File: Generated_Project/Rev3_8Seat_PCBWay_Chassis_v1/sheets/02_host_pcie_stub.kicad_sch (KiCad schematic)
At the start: 0 parts

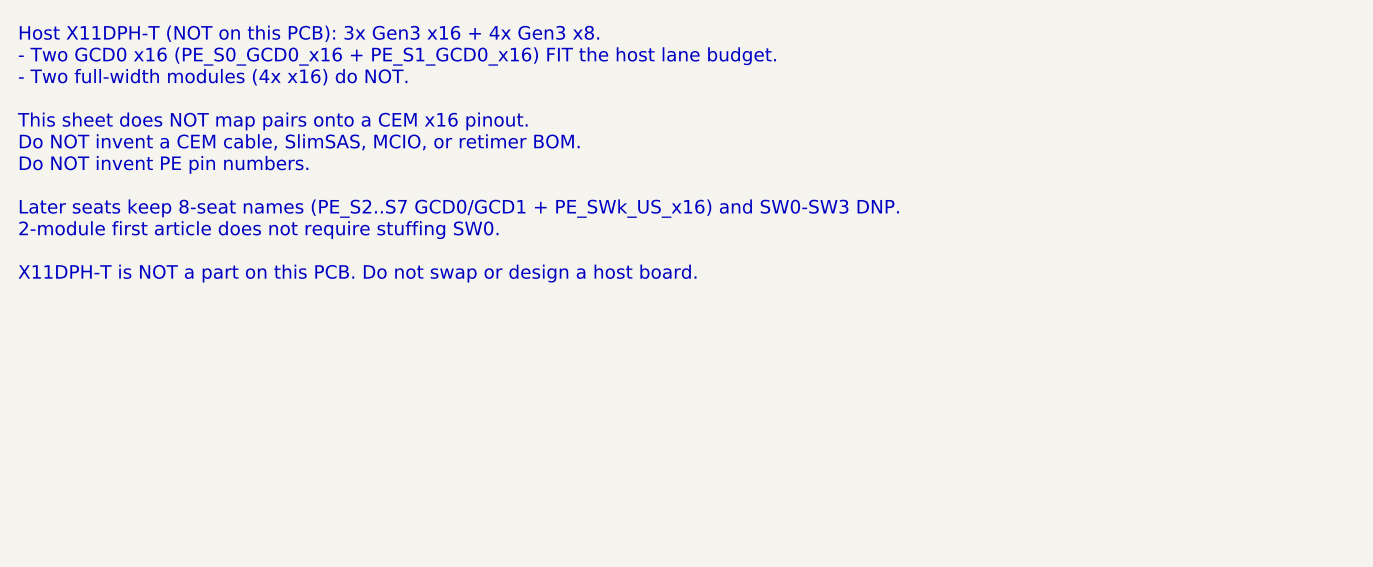
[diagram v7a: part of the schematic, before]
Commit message: Document an 8x full-width chassis CONCEPT (ideas only, not fab).
Sibling folder plus STATUS pointer. Comments-layer KiCad notes say
CONCEPT / DO NOT FABRICATE. No overlay, ball map, CEM/MCIO, r2.0, or
S1-S7 assignment. X11DPH-T cannot light 256 DS. Do not energize.
Do not upload to PCBWay.

Co-authored-by: zivzancoeli-commits <zivzancoeli-commits@users.noreply.github.com>
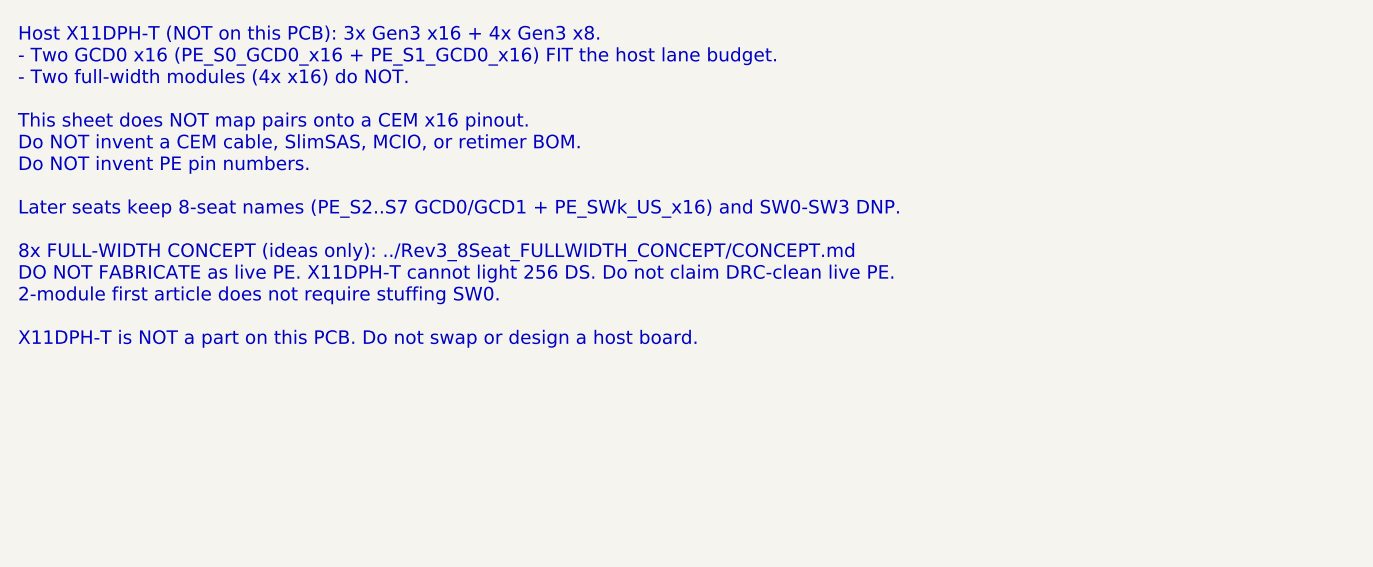
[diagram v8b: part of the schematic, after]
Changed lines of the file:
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@@
         (comment 4 "r2.0 UNUSABLE. P3V3=Conn0 C1/C2. 12L 2.0mm stuffed-switch TARGET. 4x PM8536 DNP. Star-fed P48V.")
 	)
-	(text "PURPOSE: Named v1.0 PCIE_TXnP/N and PCIE_RXnP/N (n=0..15) on ALL 8 seats.\n\nFIRST ARTICLE TARGET: seats 0 and 1. Same 8-seat PCB; 2→4→8 later.\n\nPinmap (Verified OCP v1.0 generic map + pin list; NOT an AMD overlay):\n- Conn0 PCIE_TX/RX0-15 P/N = 64 pads = PETp/n + PERp/n [15:0] \"PCIe or equivalent host link\".\n  That is the only legal named host PE today. Call it GCD0 x16 (architectural name).\n- Conn1 has ZERO PCIE_* pads. S7_* = SERDES_7 \"Reserved Link\" — 64 pads, NO NET.\n  GCD1 x16 is named-only. Do NOT assign S1-S7 as GCD1 PE.\n\nWithout overlay, \"2x MI250X\" on this zip:\n- CAN: two modules SIT on seats 0-1 (mech + named P48V/P12V1/P3V3/GND/GCD0 PE).\n- CAN target at most GCD0 on each (2 GCDs) toward the host keepout.\n- CANNOT: 2 modules at full width (4 GCDs). GCD1 pins Unknown.\n- CANNOT: light even those 2 GCD0 links until Molex 1.2 A/contact is written AND\n  a legal host connector exists. This article does not invent CEM/MCIO.\n\nHost X11DPH-T (NOT on this PCB): 3x Gen3 x16 + 4x Gen3 x8.\n- Two GCD0 x16 (PE_S0_GCD0_x16 + PE_S1_GCD0_x16) FIT the host lane budget.\n- Two full-width modules (4x x16) do NOT.\n\nThis sheet does NOT map pairs onto a CEM x16 pinout.\nDo NOT invent a CEM cable, SlimSAS, MCIO, or retimer BOM.\nDo NOT invent PE pin numbers.\n\nLater seats keep 8-seat names (PE_S2..S7 GCD0/GCD1 + PE_SWk_US_x16) and SW0-SW3 DNP.\n2-module first article does not require stuffing SW0.\n\nX11DPH-T is NOT a part on this PCB. Do not swap or design a host board.\n"
+	(text "PURPOSE: Named v1.0 PCIE_TXnP/N and PCIE_RXnP/N (n=0..15) on ALL 8 seats.\n\nFIRST ARTICLE TARGET: seats 0 and 1. Same 8-seat PCB; 2→4→8 later.\n\nPinmap (Verified OCP v1.0 generic map + pin list; NOT an AMD overlay):\n- Conn0 PCIE_TX/RX0-15 P/N = 64 pads = PETp/n + PERp/n [15:0] \"PCIe or equivalent host link\".\n  That is the only legal named host PE today. Call it GCD0 x16 (architectural name).\n- Conn1 has ZERO PCIE_* pads. S7_* = SERDES_7 \"Reserved Link\" — 64 pads, NO NET.\n  GCD1 x16 is named-only. Do NOT assign S1-S7 as GCD1 PE.\n\nWithout overlay, \"2x MI250X\" on this zip:\n- CAN: two modules SIT on seats 0-1 (mech + named P48V/P12V1/P3V3/GND/GCD0 PE).\n- CAN target at most GCD0 on each (2 GCDs) toward the host keepout.\n- CANNOT: 2 modules at full width (4 GCDs). GCD1 pins Unknown.\n- CANNOT: light even those 2 GCD0 links until Molex 1.2 A/contact is written AND\n  a legal host connector exists. This article does not invent CEM/MCIO.\n\nHost X11DPH-T (NOT on this PCB): 3x Gen3 x16 + 4x Gen3 x8.\n- Two GCD0 x16 (PE_S0_GCD0_x16 + PE_S1_GCD0_x16) FIT the host lane budget.\n- Two full-width modules (4x x16) do NOT.\n\nThis sheet does NOT map pairs onto a CEM x16 pinout.\nDo NOT invent a CEM cable, SlimSAS, MCIO, or retimer BOM.\nDo NOT invent PE pin numbers.\n\nLater seats keep 8-seat names (PE_S2..S7 GCD0/GCD1 + PE_SWk_US_x16) and SW0-SW3 DNP.\n\n8x FULL-WIDTH CONCEPT (ideas only): ../Rev3_8Seat_FULLWIDTH_CONCEPT/CONCEPT.md\nDO NOT FABRICATE as live PE. X11DPH-T cannot light 256 DS. Do not claim DRC-clean live PE.\n2-module first article does not require stuffing SW0.\n\nX11DPH-T is NOT a part on this PCB. Do not swap or design a host board.\n"
 		(exclude_from_sim no)
 		(at 20.32 20.32 0)
